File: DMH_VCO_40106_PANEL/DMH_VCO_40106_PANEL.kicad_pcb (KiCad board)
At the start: 2 copper layers, 100 x 200 mm, 35 parts, among them J1 GND

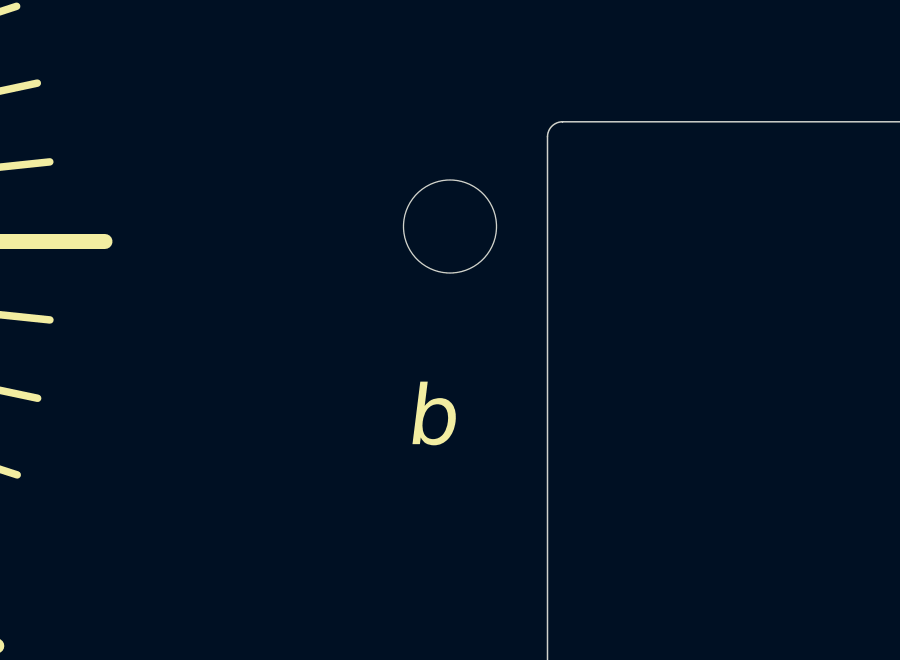
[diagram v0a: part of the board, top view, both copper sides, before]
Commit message: Removed the flat sign LED
and rerouted segments A and B to PORTD 6 and 7 respective,
and rerouted the DP segment to PORTA0
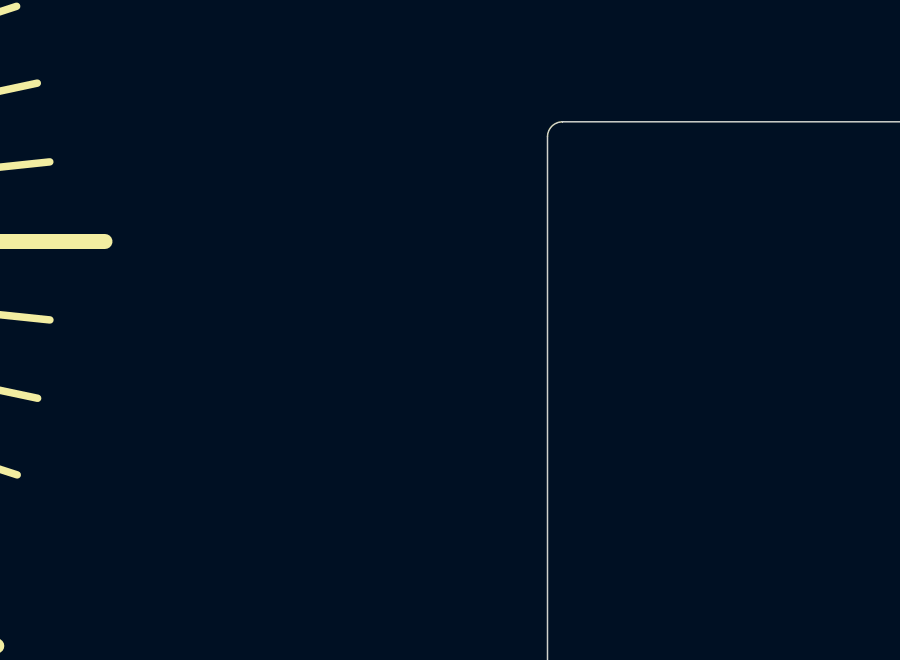
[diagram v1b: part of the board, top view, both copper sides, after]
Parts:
- removed H29: LED_b, SynthStuff:MountingHole_LED_3mm
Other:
- board text removed: "b"
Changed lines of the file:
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@@
 		)
 	)
-	(footprint "SynthStuff:MountingHole_LED_3mm"
-		(layer "F.Cu")
-		(at 119.5 91.5)
-		(descr "Mounting Hole 3mm, no annular")
-		(tags "mounting hole 3mm no annular")
-		(property "Reference" "H29"
-			(at 0 -4 0)
-			(layer "F.SilkS")
-			(hide yes)
-			(effects
-				(font
-					(size 1 1)
-					(thickness 0.15)
-				)
-			)
-		)
-		(property "Value" "LED_b"
-			(at 0 4 0)
-			(layer "F.Fab")
-			(hide yes)
-			(effects
-				(font
-					(size 1 1)
-					(thickness 0.15)
-				)
-			)
-		)
-		(property "Footprint" "SynthStuff:MountingHole_LED_3mm"
-			(at 0 0 0)
-			(unlocked yes)
-			(layer "F.Fab")
-			(hide yes)
-			(effects
-				(font
-					(size 1.27 1.27)
-					(thickness 0.15)
-				)
-			)
-		)
-		(property "Datasheet" ""
-			(at 0 0 0)
-			(unlocked yes)
-			(layer "F.Fab")
-			(hide yes)
-			(effects
-				(font
-					(size 1.27 1.27)
-					(thickness 0.15)
-				)
-			)
-		)
-		(property "Description" "Mounting Hole without connection"
-			(at 0 0 0)
-			(unlocked yes)
-			(layer "F.Fab")
-			(hide yes)
-			(effects
-				(font
-					(size 1.27 1.27)
-					(thickness 0.15)
-				)
-			)
-		)
-		(property ki_fp_filters "MountingHole*")
-		(sheetname "Root")
-		(sheetfile "DMH_VCO_40106_PANEL.kicad_sch")
-		(attr exclude_from_pos_files exclude_from_bom)
-		(fp_circle
-			(center 0 0)
-			(end 2 0)
-			(stroke
-				(width 0.15)
-				(type solid)
-			)
-			(fill none)
-			(layer "Cmts.User")
-		)
-		(fp_circle
-			(center 0 0)
-			(end 2.25 0)
-			(stroke
-				(width 0.05)
-				(type solid)
-			)
-			(fill none)
-			(layer "F.CrtYd")
-		)
-		(fp_text user "${REFERENCE}"
-			(at 0 0 0)
-			(layer "F.Fab")
-			(effects
-				(font
-					(size 1 1)
-					(thickness 0.15)
-				)
-			)
-		)
-		(pad "" np_thru_hole circle
-			(at 0 0)
-			(size 3.1 3.1)
-			(drill 3.1)
-			(layers "F&B.Cu" "*.Mask")
-		)
-	)
 	(footprint "SynthStuff:Jack_6.35mm_Cutout_v3"
 		(layer "F.Cu")
@@
 		)
 	)
-	(gr_text "b"
-		(at 118 99 0)
-		(layer "F.SilkS")
-		(effects
-			(font
-				(face "5Ceta Mono")
-				(size 2 2)
-				(thickness 0.1)
-				(italic yes)
-			)
-			(justify left bottom)
-		)
-		(render_cache "b" 0
-			(polygon
-				(pts
-					(xy 119.196789 96.198032) (xy 119.228116 96.103148) (xy 119.280454 96.018654) (xy 119.346266 95.950858)
-					(xy 119.431988 95.891342) (xy 119.531822 95.854591) (xy 119.611025 95.846322) (xy 120.633914 95.846322)
-					(xy 120.940195 96.022177) (xy 121.074528 96.198032) (xy 121.172226 96.549741) (xy 120.879623 97.95658)
-					(xy 120.635868 98.30829) (xy 120.428262 98.484145) (xy 120.048709 98.66) (xy 119.025819 98.66)
-					(xy 118.927084 98.645711) (xy 118.841206 98.597985) (xy 118.804047 98.558394) (xy 118.759235 98.468101)
-					(xy 118.750218 98.362329) (xy 118.758129 98.30829) (xy 118.684856 98.66) (xy 118 98.66) (xy 118.197835 97.708277)
-					(xy 118.896516 97.708277) (xy 118.922159 97.807277) (xy 118.950593 97.854975) (xy 119.025761 97.92076)
-					(xy 119.121084 97.953008) (xy 119.171877 97.95658) (xy 119.854291 97.95658) (xy 119.955774 97.942292)
-					(xy 120.052861 97.899427) (xy 120.115143 97.854975) (xy 120.188528 97.778258) (xy 120.240094 97.691844)
-					(xy 120.268039 97.60487) (xy 120.414096 96.901451) (xy 120.421125 96.799602) (xy 120.394168 96.701668)
-					(xy 120.364759 96.654277) (xy 120.290391 96.586594) (xy 120.196674 96.553416) (xy 120.146894 96.549741)
-					(xy 119.46448 96.549741) (xy 119.361142 96.564442) (xy 119.270881 96.603745) (xy 119.200209 96.654277)
-					(xy 119.128272 96.730428) (xy 119.077692 96.815813) (xy 119.050244 96.901451) (xy 118.904187 97.60487)
-					(xy 118.896516 97.708277) (xy 118.197835 97.708277) (xy 118.87732 94.439483) (xy 119.562177 94.439483)
-				)
-			)
-		)
-	)
 	(gr_text "On"
 		(at 129.5 65.75 0)
@@
 		)
 		(height 0)
-		(gr_text "11,2500 mm"
+		(gr_text "11.2500 mm"
 			(at 148.85 200.625 90)
 			(layer "Dwgs.User")
@@
 		)
 		(height 0)
-		(gr_text "11,2500 mm"
+		(gr_text "11.2500 mm"
 			(at 148.85 88.125 90)
 			(layer "Dwgs.User")
@@
 		)
 		(height 0)
-		(gr_text "11,2500 mm"
+		(gr_text "11.2500 mm"
 			(at 48.85 155.625 90)
 			(layer "Dwgs.User")
@@
 		)
 		(height 0)
-		(gr_text "25,0000 mm"
+		(gr_text "25.0000 mm"
 			(at 125 193.85 0)
 			(layer "Dwgs.User")
@@
 		)
 		(height 0)
-		(gr_text "11,2500 mm"
+		(gr_text "11.2500 mm"
 			(at 148.85 223.125 90)
 			(layer "Dwgs.User")
@@
 		)
 		(height 0)
-		(gr_text "11,2500 mm"
+		(gr_text "11.2500 mm"
 			(at 48.85 88.125 90)
 			(layer "Dwgs.User")
@@
 		)
 		(height 0)
-		(gr_text "22,5000 mm"
+		(gr_text "22.5000 mm"
 			(at 148.85 71.25 90)
 			(layer "Dwgs.User")
@@
 		)
 		(height 0)
-		(gr_text "11,2500 mm"
+		(gr_text "11.2500 mm"
 			(at 48.85 189.375 90)
 			(layer "Dwgs.User")
@@
 		)
 		(height 0)
-		(gr_text "11,2500 mm"
+		(gr_text "11.2500 mm"
 			(at 48.85 223.125 90)
 			(layer "Dwgs.User")
@@
 		)
 		(height 0)
-		(gr_text "11,2500 mm"
+		(gr_text "11.2500 mm"
 			(at 48.85 133.125 90)
 			(layer "Dwgs.User")
@@
 		)
 		(height 0)
-		(gr_text "25,0000 mm"
+		(gr_text "25.0000 mm"
 			(at 100 193.85 0)
 			(layer "Dwgs.User")
@@
 		)
 		(height 0)
-		(gr_text "11,2500 mm"
+		(gr_text "11.2500 mm"
 			(at 48.85 200.625 90)
 			(layer "Dwgs.User")
@@
 		)
 		(height 0)
-		(gr_text "12,5000 mm"
+		(gr_text "12.5000 mm"
 			(at 56.25 193.85 0)
 			(layer "Dwgs.User")
@@
 		)
 		(height 0)
-		(gr_text "25,0000 mm"
+		(gr_text "25.0000 mm"
 			(at 75 193.85 0)
 			(layer "Dwgs.User")

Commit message: Prepared PCBs for fabrication
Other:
- board text added: "Mk1.1 - September 2024"
- board text removed: "Mk1 - June 2024"
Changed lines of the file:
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@@
 			(usegerberattributes no)
 			(usegerberadvancedattributes no)
-			(creategerberjobfile no)
+			(creategerberjobfile yes)
 			(dashed_line_dash_ratio 12.000000)
 			(dashed_line_gap_ratio 3.000000)
@@
 			(layer "F.CrtYd")
 		)
+		(fp_rect
+			(start -8 -8)
+			(end 8 8)
+			(stroke
+				(width 0.1)
+				(type default)
+			)
+			(fill none)
+			(layer "F.Fab")
+		)
 		(fp_text user "${REFERENCE}"
 			(at 0 2.5 0)
@@
 			(layer "F.CrtYd")
 		)
+		(fp_rect
+			(start -8 -8)
+			(end 8 8)
+			(stroke
+				(width 0.1)
+				(type default)
+			)
+			(fill none)
+			(layer "F.Fab")
+		)
 		(fp_text user "${REFERENCE}"
 			(at 0 2.5 0)
@@
 			(layer "F.CrtYd")
 		)
+		(fp_rect
+			(start -8 -8)
+			(end 8 8)
+			(stroke
+				(width 0.1)
+				(type default)
+			)
+			(fill none)
+			(layer "F.Fab")
+		)
 		(fp_text user "${REFERENCE}"
 			(at 0 2.5 0)
@@
 			(layer "F.CrtYd")
 		)
+		(fp_rect
+			(start -8 -8)
+			(end 8 8)
+			(stroke
+				(width 0.1)
+				(type default)
+			)
+			(fill none)
+			(layer "F.Fab")
+		)
 		(fp_text user "${REFERENCE}"
 			(at 0 2.5 0)
@@
 			(layer "F.CrtYd")
 		)
+		(fp_rect
+			(start -8 -8)
+			(end 8 8)
+			(stroke
+				(width 0.1)
+				(type default)
+			)
+			(fill none)
+			(layer "F.Fab")
+		)
 		(fp_text user "${REFERENCE}"
 			(at 0 2.5 0)
@@
 			(layer "F.CrtYd")
 		)
+		(fp_rect
+			(start -8 -8)
+			(end 8 8)
+			(stroke
+				(width 0.1)
+				(type default)
+			)
+			(fill none)
+			(layer "F.Fab")
+		)
 		(fp_text user "${REFERENCE}"
 			(at 0 2.5 0)
@@
 			(layer "F.CrtYd")
 		)
+		(fp_rect
+			(start -8 -8)
+			(end 8 8)
+			(stroke
+				(width 0.1)
+				(type default)
+			)
+			(fill none)
+			(layer "F.Fab")
+		)
 		(fp_text user "${REFERENCE}"
 			(at 0 2.5 0)
@@
 			(layer "F.CrtYd")
 		)
+		(fp_rect
+			(start -8 -8)
+			(end 8 8)
+			(stroke
+				(width 0.1)
+				(type default)
+			)
+			(fill none)
+			(layer "F.Fab")
+		)
 		(fp_text user "${REFERENCE}"
 			(at 0 2.5 0)
@@
 			(layer "F.CrtYd")
 		)
+		(fp_rect
+			(start -8 -8)
+			(end 8 8)
+			(stroke
+				(width 0.1)
+				(type default)
+			)
+			(fill none)
+			(layer "F.Fab")
+		)
 		(fp_text user "${REFERENCE}"
 			(at 0 2.5 0)
@@
 		(layer "User.9")
 	)
-	(gr_text "Mk1 - June 2024"
+	(gr_text "Mk1.1 - September 2024"
 		(at 100 242.75 0)
 		(layer "B.SilkS")

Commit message: Replaced JLCJLCJLCJLC with space for serial number
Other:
- board text removed: "JLCJLCJLCJLC"
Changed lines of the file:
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@@
 		)
+	)
+	(gr_rect
+		(start 95 245.25)
+		(end 105 247.25)
+		(stroke
+			(width 0.1)
+			(type solid)
+		)
+		(fill solid)
+		(layer "B.SilkS")
 	)
 	(gr_line
@@
 		(layer "B.SilkS")
 		(effects
-			(font
-				(size 1.5 1.5)
-				(thickness 0.3)
-				(bold yes)
-			)
-			(justify mirror)
-		)
-	)
-	(gr_text "JLCJLCJLCJLC"
-		(at 100 246 0)
-		(layer "B.SilkS")
-		(effects

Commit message: Synced with trimpot mounting hole footprint
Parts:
- H21, H22, H23, H24: footprint MountingHole:MountingHole_2.5mm -> SynthStuff:MountingHole_TrimPot
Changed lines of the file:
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@@
 		)
 	)
-	(footprint "MountingHole:MountingHole_2.5mm"
+	(footprint "SynthStuff:MountingHole_TrimPot"
 		(layer "F.Cu")
 		(at 141.5 119.75)
@@
 		(property "Reference" "H24"
 			(at 0 -3.5 0)
-			(layer "F.SilkS")
+			(layer "F.Fab")
 			(hide yes)
 			(effects
@@
 			)
 		)
-		(property "Footprint" "MountingHole:MountingHole_2.5mm"
+		(property "Footprint" "SynthStuff:MountingHole_TrimPot"
 			(at 0 0 0)
 			(unlocked yes)
@@
 			)
 		)
-		(property "Description" "Mounting Hole without connection"
+		(property "Description" "Mounting Hole Trimpot"
 			(at 0 0 0)
 			(unlocked yes)
@@
 			(layers "*.Cu" "*.Mask")
 		)
+		(model "${KICAD8_3DMODEL_DIR}/Potentiometer_THT.3dshapes/Potentiometer_Bourns_3296W_Vertical.step"
+			(offset
+				(xyz -1.1 -1 -11.8)
+			)
+			(scale
+				(xyz 1 1 1)
+			)
+			(rotate
+				(xyz 0 0 -90)
+			)
+		)
 	)
-	(footprint "MountingHole:MountingHole_2.5mm"
+	(footprint "SynthStuff:MountingHole_TrimPot"
 		(layer "F.Cu")
 		(at 117.5 119.75)
@@
 		(property "Reference" "H21"
 			(at 0 -3.5 0)
-			(layer "F.SilkS")
+			(layer "F.Fab")
 			(hide yes)
 			(effects
@@
 			)
 		)
-		(property "Footprint" "MountingHole:MountingHole_2.5mm"
+		(property "Footprint" "SynthStuff:MountingHole_TrimPot"
 			(at 0 0 0)
 			(unlocked yes)
@@
 			)
 		)
-		(property "Description" "Mounting Hole without connection"
+		(property "Description" "Mounting Hole Trimpot"
 			(at 0 0 0)
 			(unlocked yes)
@@
 			(layers "*.Cu" "*.Mask")
 		)
+		(model "${KICAD8_3DMODEL_DIR}/Potentiometer_THT.3dshapes/Potentiometer_Bourns_3296W_Vertical.step"
+			(offset
+				(xyz -1.1 -1 -11.8)
+			)
+			(scale
+				(xyz 1 1 1)
+			)
+			(rotate
+				(xyz 0 0 -90)
+			)
+		)
 	)
-	(footprint "MountingHole:MountingHole_2.5mm"
+	(footprint "SynthStuff:MountingHole_TrimPot"
 		(layer "F.Cu")
 		(at 133.5 119.75)
@@
 		(property "Reference" "H23"
 			(at 0 -3.5 0)
-			(layer "F.SilkS")
+			(layer "F.Fab")
 			(hide yes)
 			(effects
@@
 			)
 		)
-		(property "Footprint" "MountingHole:MountingHole_2.5mm"
+		(property "Footprint" "SynthStuff:MountingHole_TrimPot"
 			(at 0 0 0)
 			(unlocked yes)
@@
 			)
 		)
-		(property "Description" "Mounting Hole without connection"
+		(property "Description" "Mounting Hole Trimpot"
 			(at 0 0 0)
 			(unlocked yes)
@@
 			(layers "*.Cu" "*.Mask")
 		)
+		(model "${KICAD8_3DMODEL_DIR}/Potentiometer_THT.3dshapes/Potentiometer_Bourns_3296W_Vertical.step"
+			(offset
+				(xyz -1.1 -1 -11.8)
+			)
+			(scale
+				(xyz 1 1 1)
+			)
+			(rotate
+				(xyz 0 0 -90)
+			)
+		)
 	)
 	(footprint "SynthStuff:Jack_6.35mm_Cutout_Output_v6"
@@
 		)
 	)
-	(footprint "MountingHole:MountingHole_2.5mm"
+	(footprint "SynthStuff:MountingHole_TrimPot"
 		(layer "F.Cu")
 		(at 125.5 119.75)
@@
 		(property "Reference" "H22"
 			(at 0 -3.5 0)
-			(layer "F.SilkS")
+			(layer "F.Fab")
 			(hide yes)
 			(effects
@@
 			)
 		)
-		(property "Footprint" "MountingHole:MountingHole_2.5mm"
+		(property "Footprint" "SynthStuff:MountingHole_TrimPot"
 			(at 0 0 0)
 			(unlocked yes)
@@
 			)
 		)
-		(property "Description" "Mounting Hole without connection"
+		(property "Description" "Mounting Hole Trimpot"
 			(at 0 0 0)
 			(unlocked yes)
@@
 			(layers "*.Cu" "*.Mask")
 		)
+		(model "${KICAD8_3DMODEL_DIR}/Potentiometer_THT.3dshapes/Potentiometer_Bourns_3296W_Vertical.step"
+			(offset
+				(xyz -1.1 -1 -11.8)
+			)
+			(scale
+				(xyz 1 1 1)
+			)
+			(rotate
+				(xyz 0 0 -90)
+			)
+		)
 	)

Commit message: Fixed resistor values and regenerated gerbers
New gerbers version: Mk1.2
Includes fix with small font problem with the # sign under the blue LED on the front panel.
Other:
- board text added: "Mk1.2 - October 2024"
- board text removed: "Mk1.1 - September 2024"
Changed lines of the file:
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@@
 		(layer "User.9")
 	)
-	(gr_text "Mk1.1 - September 2024"
+	(gr_text "Mk1.2 - October 2024"
 		(at 100 242.75 0)
 		(layer "B.SilkS")
@@
 		)
 		(height 0)
-		(gr_text "11.2500 mm"
+		(gr_text "11,2500 mm"
 			(at 148.85 200.625 90)
 			(layer "Cmts.User")
@@
 		)
 		(height 0)
-		(gr_text "11.2500 mm"
+		(gr_text "11,2500 mm"
 			(at 148.85 88.125 90)
 			(layer "Cmts.User")
@@
 		)
 		(height 0)
-		(gr_text "11.2500 mm"
+		(gr_text "11,2500 mm"
 			(at 48.85 155.625 90)
 			(layer "Cmts.User")
@@
 		)
 		(height 0)
-		(gr_text "25.0000 mm"
+		(gr_text "25,0000 mm"
 			(at 125 193.85 0)
 			(layer "Cmts.User")
@@
 		)
 		(height 0)
-		(gr_text "11.2500 mm"
+		(gr_text "11,2500 mm"
 			(at 148.85 223.125 90)
 			(layer "Cmts.User")
@@
 		)
 		(height 0)
-		(gr_text "11.2500 mm"
+		(gr_text "11,2500 mm"
 			(at 48.85 88.125 90)
 			(layer "Cmts.User")
@@
 		)
 		(height 0)
-		(gr_text "22.5000 mm"
+		(gr_text "22,5000 mm"
 			(at 148.85 71.25 90)
 			(layer "Cmts.User")
@@
 		)
 		(height 0)
-		(gr_text "11.2500 mm"
+		(gr_text "11,2500 mm"
 			(at 48.85 189.375 90)
 			(layer "Cmts.User")
@@
 		)
 		(height 0)
-		(gr_text "11.2500 mm"
+		(gr_text "11,2500 mm"
 			(at 48.85 223.125 90)
 			(layer "Cmts.User")
@@
 		)
 		(height 0)
-		(gr_text "11.2500 mm"
+		(gr_text "11,2500 mm"
 			(at 48.85 133.125 90)
 			(layer "Cmts.User")
@@
 		)
 		(height 0)
-		(gr_text "25.0000 mm"
+		(gr_text "25,0000 mm"
 			(at 100 193.85 0)
 			(layer "Cmts.User")
@@
 		)
 		(height 0)
-		(gr_text "11.2500 mm"
+		(gr_text "11,2500 mm"
 			(at 48.85 200.625 90)
 			(layer "Cmts.User")
@@
 		)
 		(height 0)
-		(gr_text "12.5000 mm"
+		(gr_text "12,5000 mm"
 			(at 56.25 193.85 0)
 			(layer "Cmts.User")
@@
 		)
 		(height 0)
-		(gr_text "25.0000 mm"
+		(gr_text "25,0000 mm"
 			(at 75 193.85 0)
 			(layer "Cmts.User")
